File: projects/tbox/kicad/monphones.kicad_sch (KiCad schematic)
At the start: 77 parts, among them J601 PHONES 3.5, J602 PHONES 1/4, J603 PHONES 3.5, J604 PHONES 1/4, U601 OPA1678, U602 OPA1678, U603 NJM4556A, U604 NJM4556A

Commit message: Re-cut the hierarchy by board: front / control / rear sheets, ribbons on the root
The functional sheets no longer map to the physical boards, so the root
now holds one sheet per PCB and the wires on it are the two ribbon
cables.  The control board is parallel to the 13-degree top slope, so
the front jacks need their own vertical board; the preamps go with them
so mic level never crosses a connector.

- keying -> Keying Logic (control) + Rear I/O (rear)
  txbus  -> TX Sum / Intercom (control) + Rig Out (rear)
  rxphones -> Monitor / Phones (control) + RX In (rear); phones jacks
  redrawn on the Front board.  Preamp loses its level pot (redrawn on
  TX Sum) and is instanced under the Front board; Supply under Rear.
- Cross-board nets are hierarchical labels threaded through sheet pins
  and the ribbon connectors J901/J902 (front-control) and J903/J904
  (control-rear), 2x13 IDC, straight-through, GND on every third pin;
  GAIN/BIAS pass through the control board.  Rails ride the ribbons as
  power symbols with local decoupling at each connector.
- Two deliberate net changes: the front PTT buttons now sit after the
  jack beads (PTT_x_IN), and phones jack sleeves plus the TRRS common
  return to board GND instead of CHASSIS -- a chassis return would put
  headphone current through the single tie and the rear ribbon ground,
  in series with the mic reference.  Every other net is unchanged
  (netlist partition verified: 209 nets, only those two differ).
- tools/check_boards.py: every net spanning two boards must pass
  through a ribbon connector on each; both ends of each ribbon must
  carry the same net pin for pin.  It caught the pass-through nets being
  control-local labels on the first cut.
- Panel-mount Powerpole to J1; side view gains the front board; DESIGN
  mechanical section rewritten; CLAUDE.md hierarchy rule; TODO layout
  items (snap-apart panel, ribbon DRC exclusions).
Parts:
- removed C601, C602: 10u, symbol Device:C_Polarized
- removed C614: 100n, symbol Device:C
- removed C618, C619: 47u, symbol Device:C_Polarized
- removed C622, C623: 100p, symbol Device:C
- removed J601, J603: PHONES 3.5, symbol Connector_Audio:AudioJack3
- removed J602, J604: PHONES 1/4, symbol Connector_Audio:AudioJack3
- removed R601, R602, R605, R606: 10k, symbol Device:R
- removed R603, R607: 47k, symbol Device:R
- removed R604, R608, R635, R636: 100R, symbol Device:R
- removed R633, R634: 100k, symbol Device:R
- removed RV601, RV602: 10k, symbol Device:R_Potentiometer_Trim
- removed TP601: RX_L_BUS, symbol Connector:TestPoint
- removed TP602: RX_R_BUS, symbol Connector:TestPoint
- removed U601: OPA1678, symbol tbox:OPA1678
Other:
- note added: "Each ear: RX side + MON summed passively (10k+10k into the 10k volume gang, -9.5 dB) -> NJM4556A +24 dB -> 10R -> 470u -> bead + 10n -> PH_x_L/R over the ribbon to the front-board jacks (sleeves to GND)."
- note added: "Hierarchical: RX_x_BUS from the rear board (ribbon); PH_x_L/R to the front board (ribbon). TX_MON is board-local from TX Sum."
- note added: "Monitor / phones (control board) -- MON pots and buffers, per-ear passive mix, VOL, NJM4556A headphone amps -> front-board jacks."
- note removed: "+15 dB (1 + 47k/10k), unity at DC (C618/C619); trims to GND, +in biased to VREF via 100k (VREF noise gain ~1); R635/C622 RF stop at the pin"
- note removed: "Each ear: RX side + MON summed passively (10k+10k into the 10k volume gang, -9.5 dB) -> NJM4556A +24 dB -> 10R -> 470u -> bead + 10n -> jacks; sleeves to CHASSIS."
- note removed: "Global nets: RX_L_IN/RX_R_IN from Keying+Rear; TX_MON from TX Bus; RX_x_BUS to TX Bus line-out select; PH_x_L/R to the preamp TRRS jacks."
- note removed: "Max ~-0.4 dBV open (17 mW/32R, 22 mW/16R through the 10R build-out; one headset per position). 3.5 mm, 1/4" and the TRRS phones side (J203/J303 on the preamp sheets, via PH_x_L/R) are paralleled."
- note removed: "Mono rig cables tie RX L and RX R at the DE-9 (Keying+Rear sheet, with the filter/clamp)."
- note removed: "RX in: 10k bridging load, rear 10k trim to GND (hot phones-jack sources are simply trimmed down), AC-coupled into a +15 dB buffer -> RX_L_BUS / RX_R_BUS at -15 dBV."
- note removed: "RX inputs, monitor buffers, headphone mixers/amps (positions A and B)."
- title: TBox — RX Inputs / Monitor / Headphones -> TBox — Monitor / Phones (control board)

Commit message: Annotate by board: KiCad annotator, first free after sheet number x100 (1xxx front, 2xxx control, 3xxx rear)
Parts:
- renumbered C603 to C2401, C605 to C2402, C604 to C2403, C606 to C2404, C620 to C2405, C615 to C2406, C621 to C2407, C607 to C2408, C609 to C2409, C616 to C2410, C608 to C2411, C610 to C2412, C617 to C2413, FB601 to FB2401, FB602 to FB2402, FB603 to FB2403, FB604 to FB2404, R609 to R2401, R610 to R2402, R615 to R2403, R616 to R2404, R611 to R2405, R617 to R2406, R612 to R2407, R618 to R2408, R613 to R2409, R619 to R2410, R614 to R2411, R620 to R2412, R621 to R2413, R622 to R2414, R627 to R2415, R628 to R2416, R623 to R2417, R629 to R2418, R624 to R2419, R630 to R2420, R625 to R2421, R631 to R2422, R626 to R2423, R632 to R2424, RV604 to RV2401, RV603 to RV2402, RV605 to RV2403, RV606 to RV2404, TP603 to TP2401, U603 to U2401, U602 to U2402, U604 to U2403

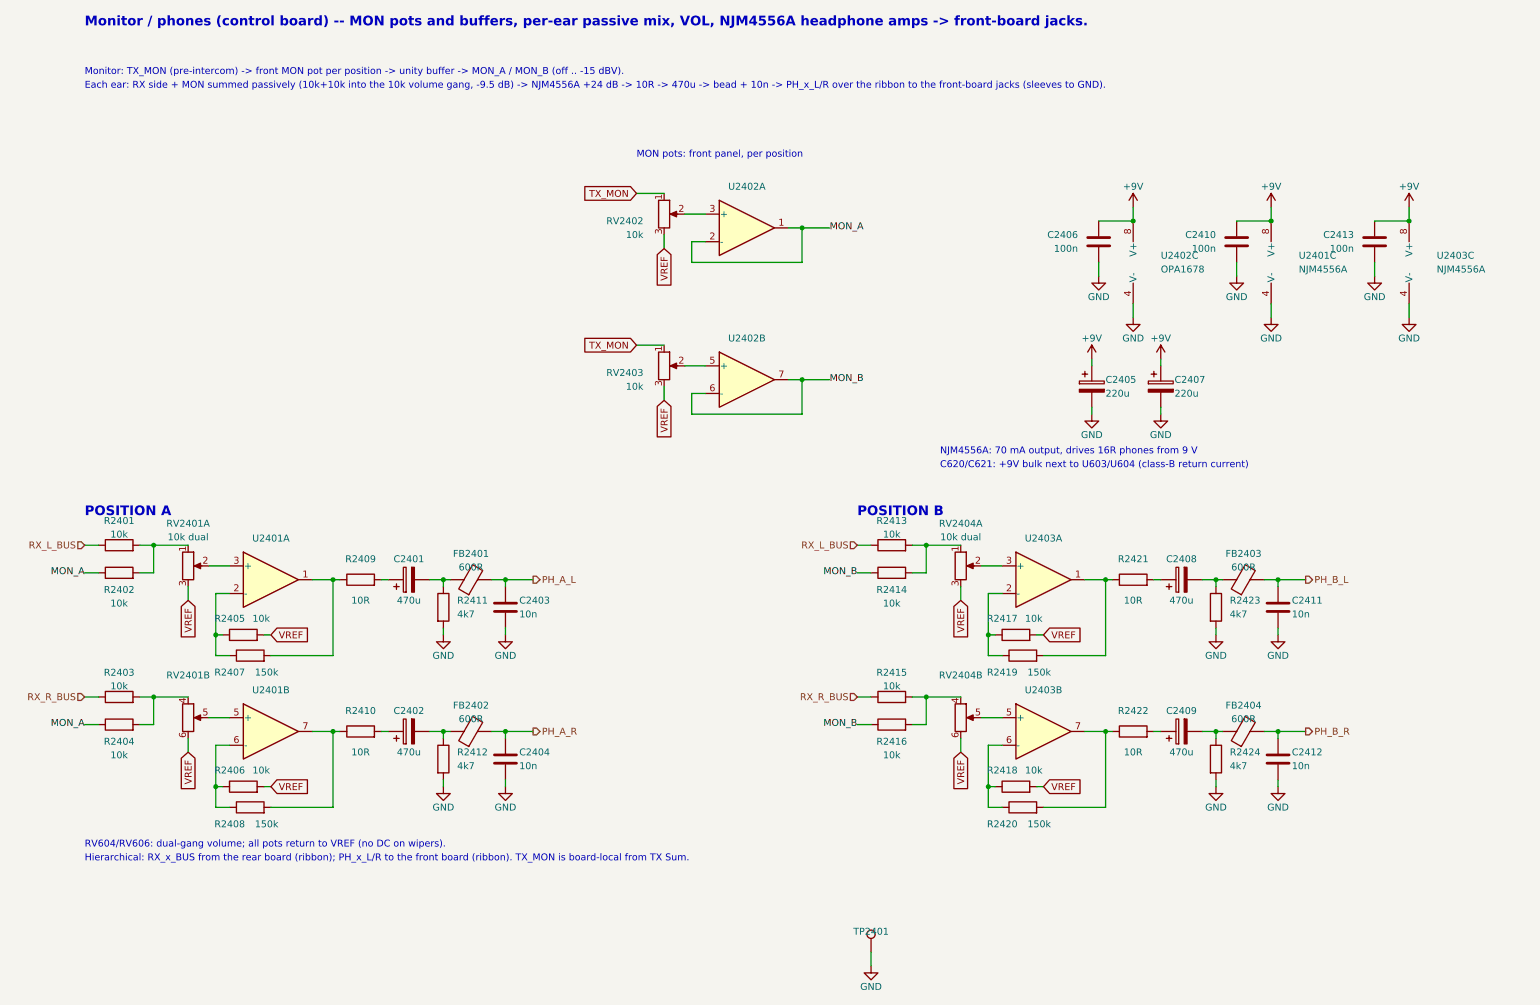
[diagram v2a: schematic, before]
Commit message: Rename refdes mentions in notes and docs to the board-coded numbering
Table-driven: the old->new map was derived from symbol UUIDs across the
annotation commit (619 instances, checked one-to-one and per board), and
only exact whole tokens from that table were replaced, in sheet notes,
connector Values, DESIGN.md, TODO.md and power_tree.json.  The one range
("J901-J904") and the one instance-specific ref in the shared Mute sheet
were rewritten by hand.  Power tree regenerated (loads now grouped by
board).  Netlist identical to the annotated baseline.
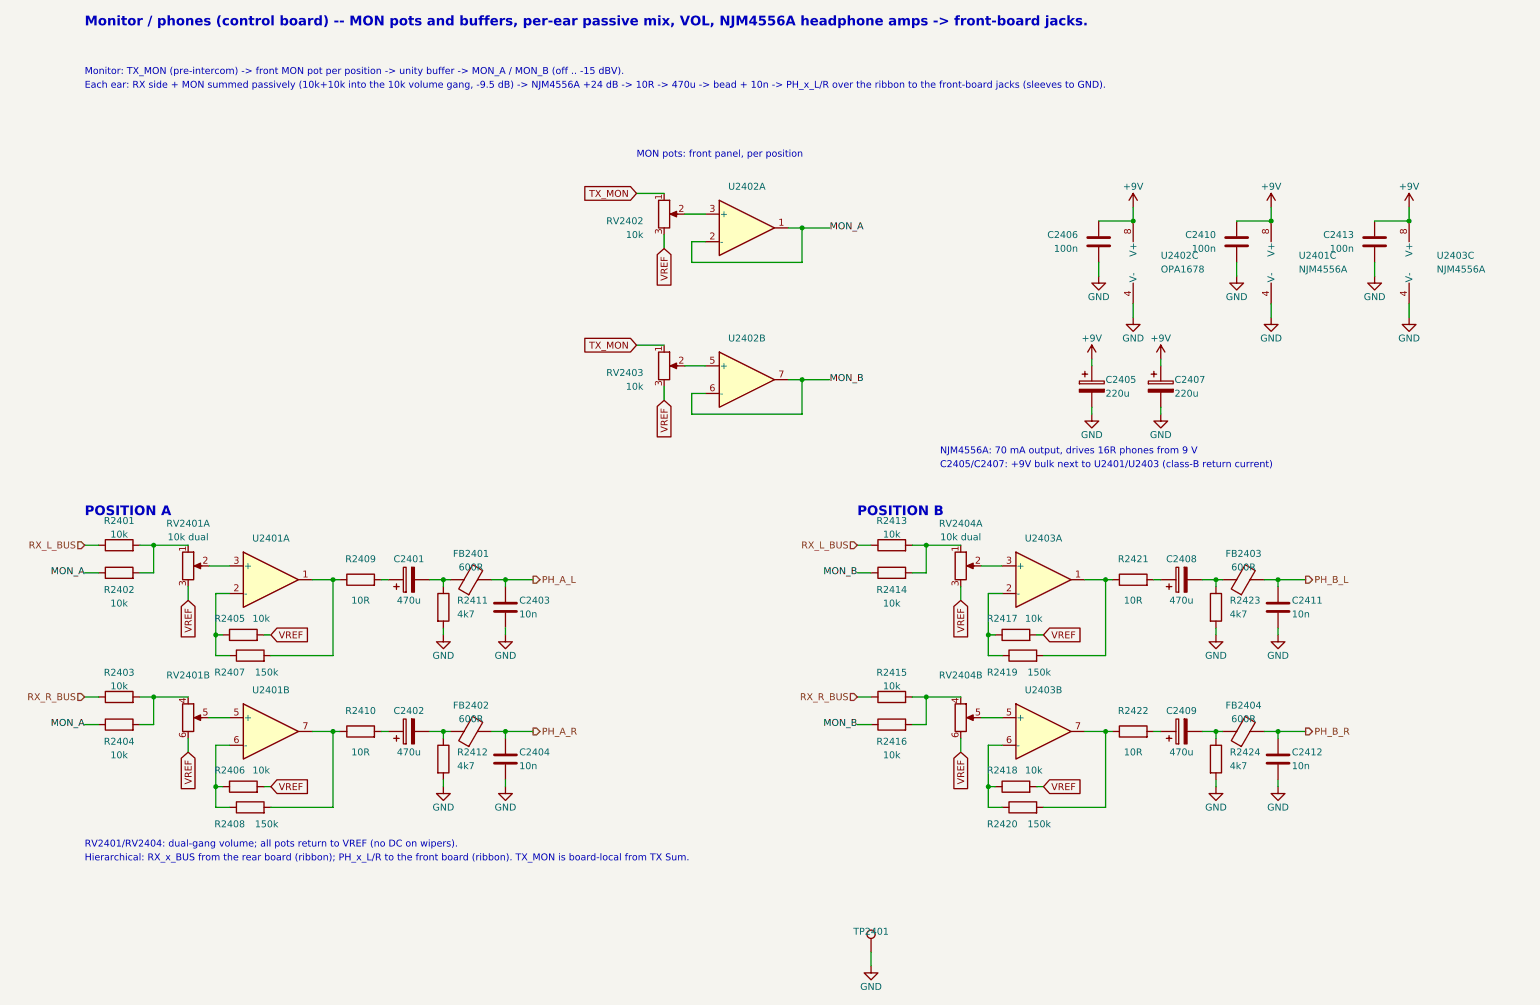
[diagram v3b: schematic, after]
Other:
- note added: "C2405/C2407: +9V bulk next to U2401/U2403 (class-B return current)"
- note added: "RV2401/RV2404: dual-gang volume; all pots return to VREF (no DC on wipers)."
- note removed: "C620/C621: +9V bulk next to U603/U604 (class-B return current)"
- note removed: "RV604/RV606: dual-gang volume; all pots return to VREF (no DC on wipers)."
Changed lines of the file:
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@@
 		)
 	)
-	(text "RV604/RV606: dual-gang volume; all pots return to VREF (no DC on wipers)."
+	(text "RV2401/RV2404: dual-gang volume; all pots return to VREF (no DC on wipers)."
 		(exclude_from_sim no)
 		(at 20.32 171.45 0)
@@
 		)
 	)
-	(text "C620/C621: +9V bulk next to U603/U604 (class-B return current)"
+	(text "C2405/C2407: +9V bulk next to U2401/U2403 (class-B return current)"
 		(exclude_from_sim no)
 		(at 177.8 101.6 0)

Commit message: Footprint pass: every board part has a footprint, chosen parts carry MPNs
0603 base for R and C <= 1 uF, 0805 for 4u7, 1206 for 10 uF ceramics
(including the three non-polar coupling caps), 1210 for the 47 uF X7R;
electrolytics by can size; Keystone 5015 test points.  Panel parts per
the discussion: Switchcraft 35RAPC(2A/2B)H3 and Neutrik NRJ6HM-1-PRE
where the sleeve must bond to the panel, CUI SJ1-353xNG and Rean
NRJ6HF-1 where it must not; Alpha 9 mm pots, Bourns 3386 side-adjust
trims, C&K 7101 AV2 / 7201 V-bracket toggles, C&K PVA buttons, IDC
2x13 headers (vertical on front/rear, right-angle on control), JST XH
for the Powerpole pigtail (through-hole on purpose), Triad TY-250P
transformers, 0805 LEDs with light pipes.  J3207 (GND post) is a
panel part: on_board no.

kicad/tbox.pretty holds the four footprints with no stock equivalent,
each drawn from the vendor drawing and saying so in its description:
Switchcraft 35RAPC__H3 (rev J), C&K 7101 AV2 and 7201 V-bracket
patterns, Triad TY-250P (pads mapped to the Transformer_1P_1S symbol,
6-7 tied on copper for 1:1).

tools/check_footprints.py enforces the invariant.  Netlist unchanged
apart from J3207 leaving the board.
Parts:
- C2401, C2402, C2408, C2409: footprint (none) -> Capacitor_SMD:CP_Elec_10x10.5
- C2403, C2404, C2406, C2410, C2411, C2412, C2413: footprint (none) -> Capacitor_SMD:C_0603_1608Metric
- C2405, C2407: footprint (none) -> Capacitor_SMD:CP_Elec_8x10.5
- FB2401, FB2402, FB2403, FB2404: footprint (none) -> Inductor_SMD:L_0805_2012Metric
- R2401, R2402, R2403, R2404, R2405, R2406, R2407, R2408, R2409, R2410, R2411, R2412, R2413, R2414, R2415, R2416, R2417, R2418, R2419, R2420, R2421, R2422, R2423, R2424: footprint (none) -> Resistor_SMD:R_0603_1608Metric
- RV2401, RV2404: footprint (none) -> Potentiometer_THT:Potentiometer_Alpha_RD902F-40-00D_Dual_Vertical; MPN (none) -> RD902F-40-15R1-A10K
- RV2402, RV2403: footprint (none) -> Potentiometer_THT:Potentiometer_Alpha_RD901F-40-00D_Single_Vertical; MPN (none) -> RD901F-40-15R1-A10K
- TP2401: footprint (none) -> TestPoint:TestPoint_Keystone_5015_Micro_Mini; MPN (none) -> 5015
- U2401, U2403: footprint (none) -> Package_SO:SOIC-8_3.9x4.9mm_P1.27mm; MPN (none) -> NJM4556AM
- U2402: footprint (none) -> Package_SO:SOIC-8_3.9x4.9mm_P1.27mm; MPN (none) -> OPA1678IDR
